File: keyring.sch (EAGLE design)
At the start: 7 parts, among them IC1 ATMEGA8-PU, T1 2N2222, X1 22-23-2031

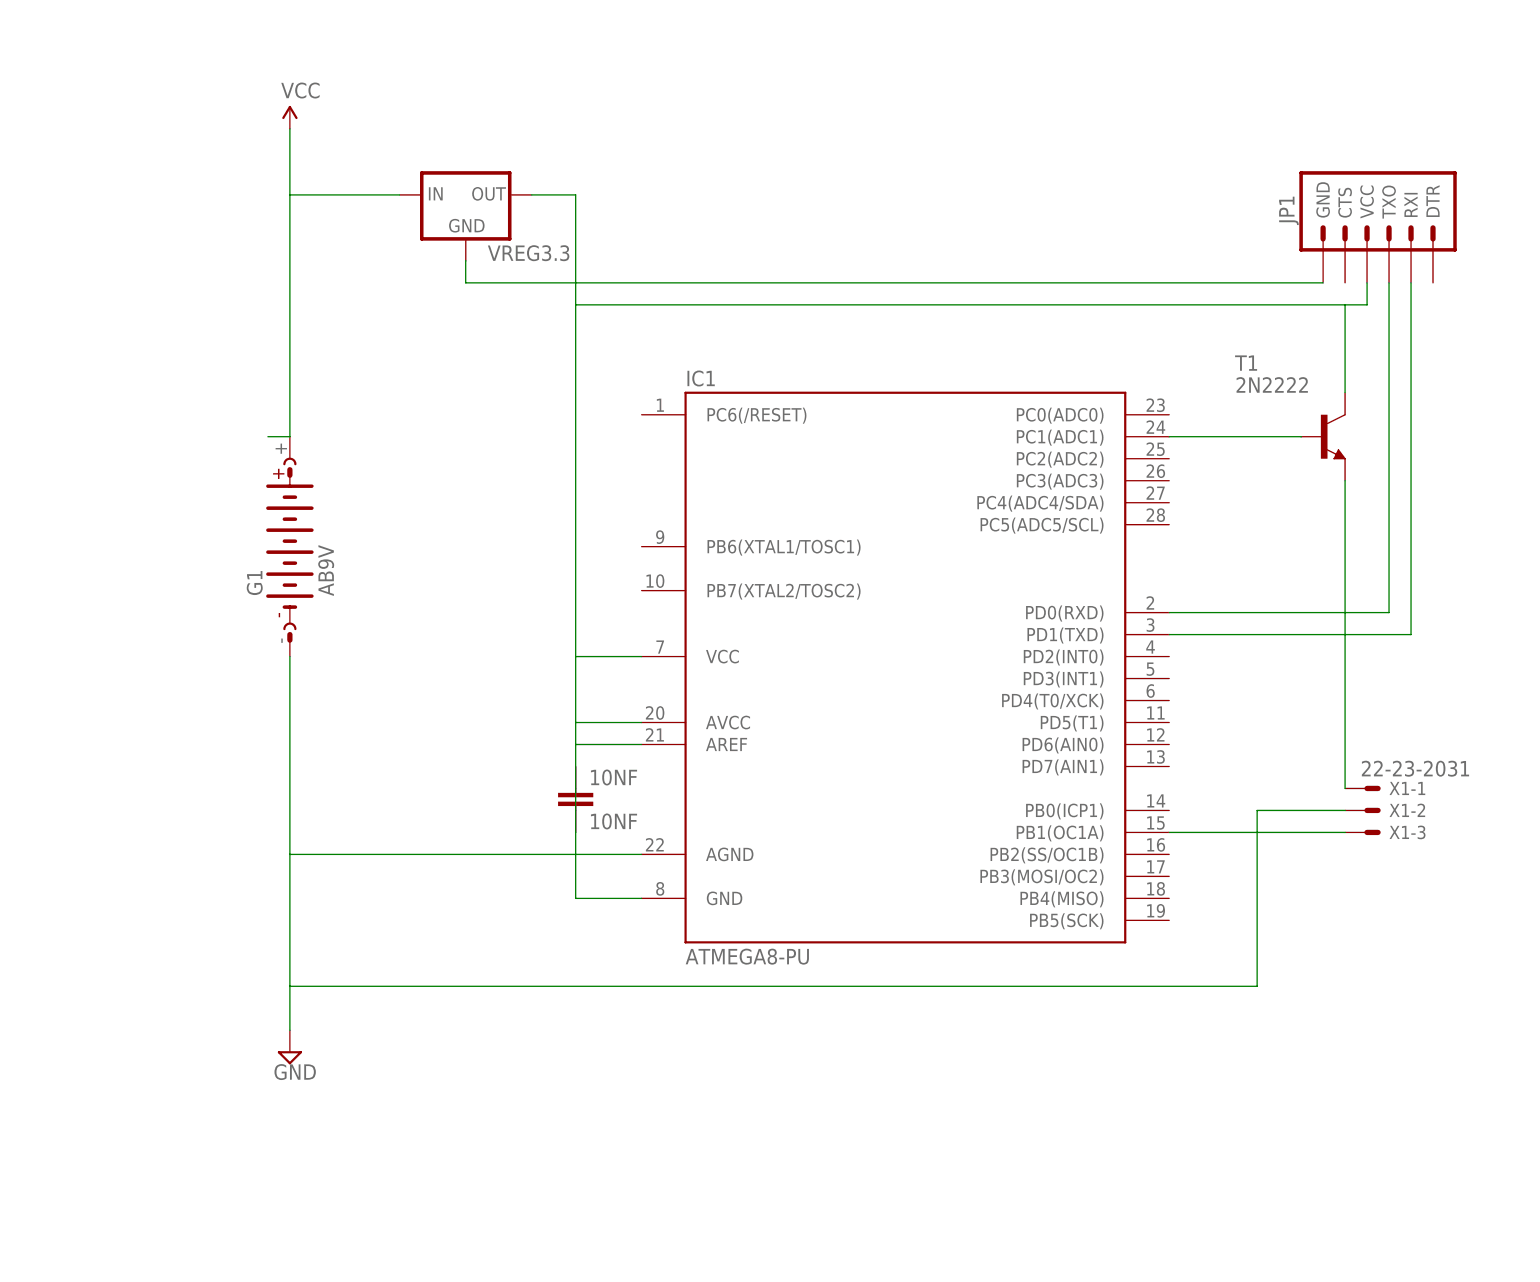
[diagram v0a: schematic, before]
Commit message: bigger pads
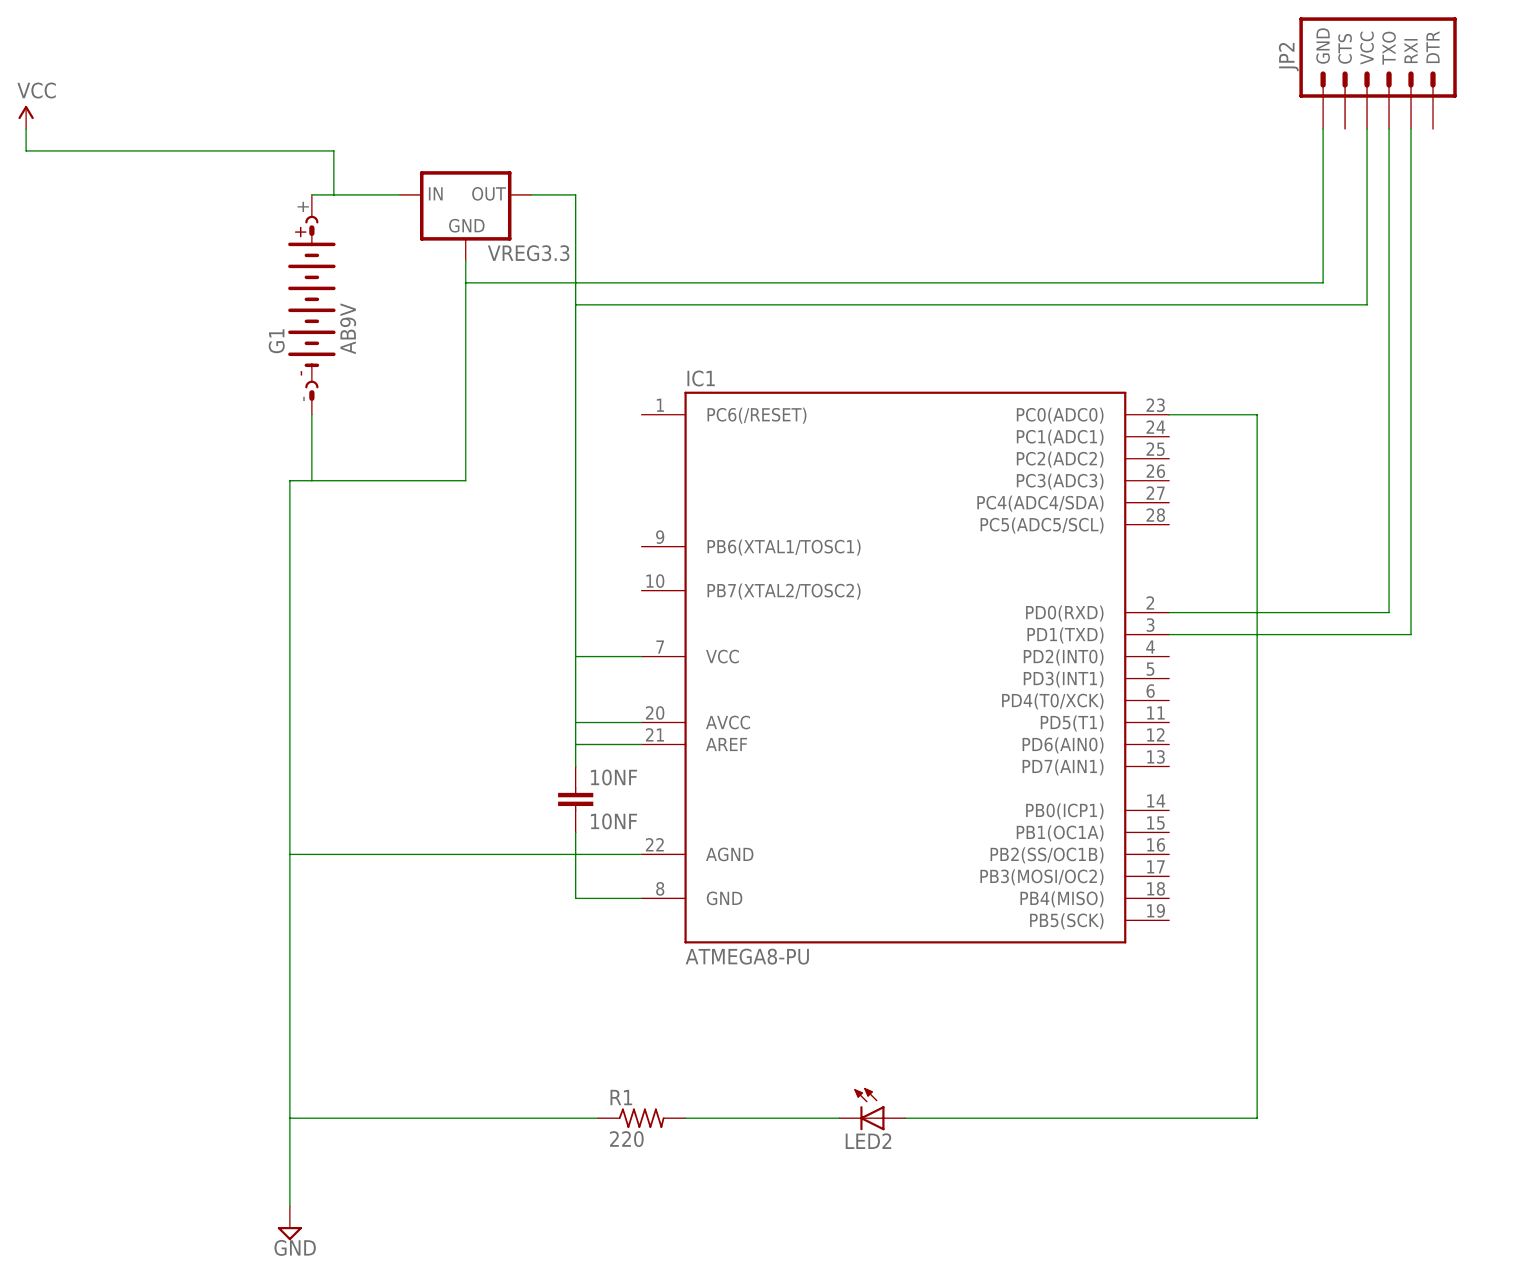
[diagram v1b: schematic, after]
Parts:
- removed JP1: (no value), SparkFun:ARDUINO_SERIAL_PROGRAMPTH
- removed T1: 2N2222, adafruit:2N2222
- removed X1: 22-23-2031, con-molex:22-23-2031
- added JP2: (no value), SparkFun:ARDUINO_SERIAL_PROGRAMLONGPADS
- added LED2: (no value), led:LED3MM
- added R1: 220, resistor:R-US_0207/12
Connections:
- removed net N$1: VREG3.3.GND
- removed net N$4: IC1.PC1(ADC1), T1.B
- removed net N$6: IC1.PB1(OC1A), X1-3.S
- new net N$7: LED2.C, R1.2
- new net N$8: 10NF.1, IC1.AREF, IC1.AVCC, IC1.VCC@1, JP2.VCC, VREG3.3.OUT
- net GND: now also JP2.GND, R1.1, VREG3.3.GND; no longer IC1.AREF, IC1.AVCC, IC1.VCC@1, JP1.VCC, T1.C, VREG3.3.OUT, X1-2.S
- net N$2: now also JP2.RXI; no longer JP1.RXI
- net N$3: now also JP2.TXO; no longer JP1.TXO
- net N$5: now also IC1.PC0(ADC0), LED2.A; no longer T1.E, X1-1.S
- net VCC: now also G1.+
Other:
- moved on the sheet: G1

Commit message: added keyboard
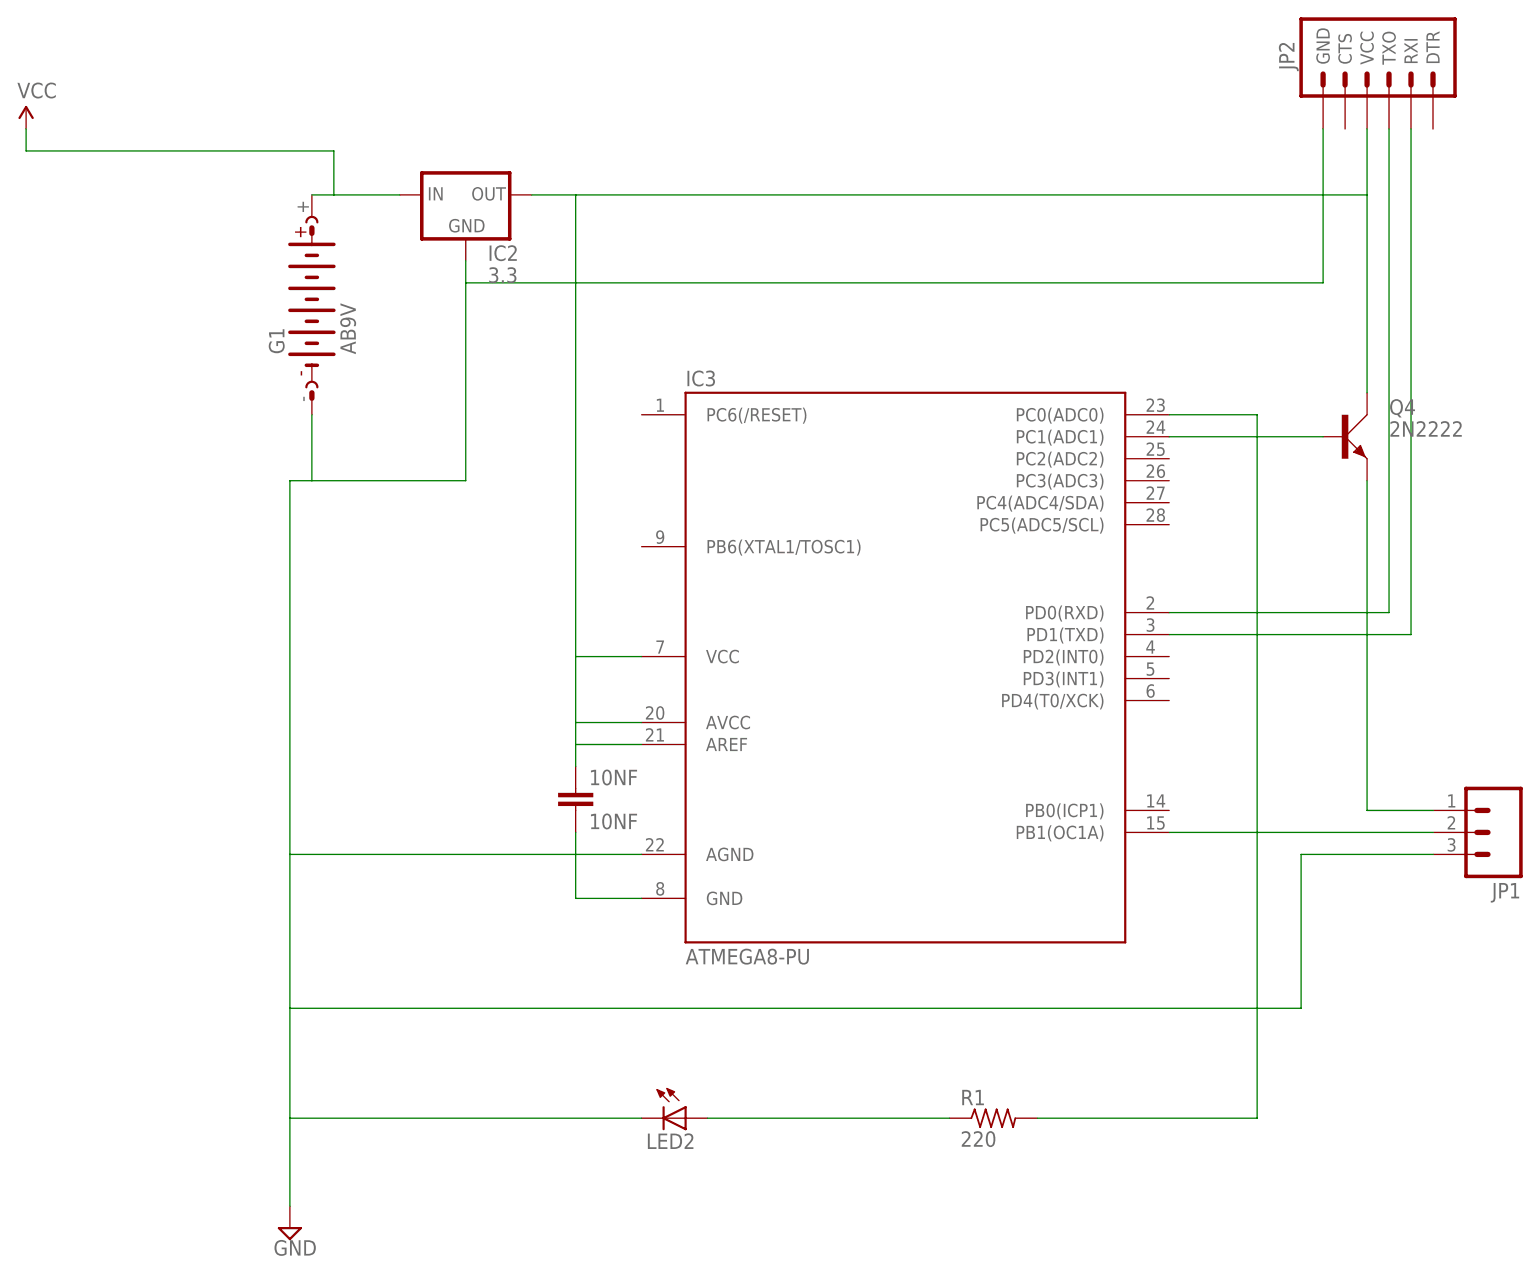
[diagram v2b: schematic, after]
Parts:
- removed IC1: ATMEGA8-PU, atmega8:ATMEGA8-PU
- added IC3: ATMEGA8-PU, atmega8 uden ben:ATMEGA8-PU
- added JP1: (no value), SparkFun:M03LONGPADS
- added Q4: 2N2222, transistor-small-signal:2N2222
- IC2: value (none) -> 3.3
- renumbered VREG3.3 to IC2
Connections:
- removed net GND: 10NF.2, G1.-, IC1.AGND, IC1.GND@1, IC2.GND, JP2.GND, R1.1
- new net N$1: IC3.PC1(ADC1), Q4.B
- new net N$10: 10NF.2, G1.-, IC2.GND, IC3.AGND, IC3.GND@1, JP1.VCC, JP2.GND, LED2.C
- new net N$4: JP1.OUT, Q4.E
- new net N$6: IC3.PB1(OC1A), JP1.GND
- net N$2: now also IC3.PD1(TXD); no longer IC1.PD1(TXD)
- net N$3: now also IC3.PD0(RXD); no longer IC1.PD0(RXD)
- net N$5: now also IC3.PC0(ADC0), R1.2; no longer IC1.PC0(ADC0), LED2.A
- net N$7: now also LED2.A, R1.1; no longer LED2.C, R1.2
- net N$8: now also IC3.AREF, IC3.AVCC, IC3.VCC@1, Q4.C; no longer IC1.AREF, IC1.AVCC, IC1.VCC@1
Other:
- moved on the sheet: LED2, R1
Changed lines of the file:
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@@
 </classes>
 <parts>
-<part name="IC1" library="atmega8" deviceset="ATMEGA8-PU" device=""/>
-<part name="VREG3.3" library="SparkFun" deviceset="V_REG_78XX" device="SINK"/>
 <part name="BATTERY" library="SparkFun" deviceset="VCC" device=""/>
 <part name="SUPPLY1" library="supply2" deviceset="GND" device=""/>
@@
 <part name="LED2" library="led" deviceset="LED" device="3MM"/>
 <part name="JP2" library="SparkFun" deviceset="ARDUINO_SERIAL_PROGRAM" device="LONGPADS"/>
+<part name="IC2" library="SparkFun" deviceset="V_REG_78XX" device="SINK" value="3.3"/>
+<part name="JP1" library="SparkFun" deviceset="M03" device="LONGPADS"/>
+<part name="IC3" library="atmega8 uden ben" deviceset="ATMEGA8-PU" device=""/>
+<part name="Q4" library="transistor-small-signal" deviceset="2N2222" device=""/>
 </parts>
 <sheets>
@@
 </plain>
 <instances>
-<instance part="IC1" gate="1" x="71.12" y="15.24"/>
-<instance part="VREG3.3" gate="G$1" x="20.32" y="68.58"/>
 <instance part="BATTERY" gate="1" x="-30.48" y="76.2"/>
 <instance part="SUPPLY1" gate="GND" x="0" y="-50.8"/>
 <instance part="10NF" gate="G$1" x="33.02" y="0"/>
 <instance part="G1" gate="G$1" x="2.54" y="55.88" rot="R90"/>
-<instance part="R1" gate="G$1" x="40.64" y="-38.1"/>
-<instance part="LED2" gate="G$1" x="68.58" y="-38.1" rot="R270"/>
+<instance part="R1" gate="G$1" x="81.28" y="-38.1"/>
+<instance part="LED2" gate="G$1" x="45.72" y="-38.1" rot="R270"/>
 <instance part="JP2" gate="G$1" x="127" y="81.28" rot="MR270"/>
+<instance part="IC2" gate="G$1" x="20.32" y="68.58"/>
+<instance part="JP1" gate="G$1" x="139.7" y="-5.08" rot="R180"/>
+<instance part="IC3" gate="1" x="71.12" y="15.24"/>
+<instance part="Q4" gate="1" x="121.92" y="40.64"/>
 </instances>
 <busses>
@@
 <wire x1="-30.48" y1="73.66" x2="5.08" y2="73.66" width="0.1524" layer="91"/>
 <wire x1="5.08" y1="73.66" x2="5.08" y2="68.58" width="0.1524" layer="91"/>
-<pinref part="VREG3.3" gate="G$1" pin="IN"/>
 <wire x1="5.08" y1="68.58" x2="12.7" y2="68.58" width="0.1524" layer="91"/>
 <pinref part="G1" gate="G$1" pin="+"/>
 <wire x1="2.54" y1="68.58" x2="5.08" y2="68.58" width="0.1524" layer="91"/>
+<pinref part="IC2" gate="G$1" pin="IN"/>
 </segment>
 </net>
-<net name="GND" class="0">
+<net name="N$10" class="0">
 <segment>
 <pinref part="SUPPLY1" gate="GND" pin="GND"/>
 <wire x1="0" y1="35.56" x2="0" y2="-7.62" width="0.1524" layer="91"/>
-<wire x1="0" y1="-7.62" x2="0" y2="-38.1" width="0.1524" layer="91"/>
-<pinref part="IC1" gate="1" pin="AGND"/>
+<wire x1="0" y1="-7.62" x2="0" y2="-25.4" width="0.1524" layer="91"/>
+<wire x1="0" y1="-25.4" x2="0" y2="-38.1" width="0.1524" layer="91"/>
 <wire x1="0" y1="-38.1" x2="0" y2="-48.26" width="0.1524" layer="91"/>
 <wire x1="40.64" y1="-7.62" x2="33.02" y2="-7.62" width="0.1524" layer="91"/>
 <wire x1="33.02" y1="-7.62" x2="0" y2="-7.62" width="0.1524" layer="91"/>
-<pinref part="IC1" gate="1" pin="GND@1"/>
 <wire x1="40.64" y1="-12.7" x2="33.02" y2="-12.7" width="0.1524" layer="91"/>
 <wire x1="33.02" y1="-12.7" x2="33.02" y2="-7.62" width="0.1524" layer="91"/>
@@
 <wire x1="33.02" y1="-5.08" x2="33.02" y2="-7.62" width="0.1524" layer="91"/>
 <wire x1="0" y1="35.56" x2="2.54" y2="35.56" width="0.1524" layer="91"/>
-<pinref part="VREG3.3" gate="G$1" pin="GND"/>
 <wire x1="2.54" y1="35.56" x2="20.32" y2="35.56" width="0.1524" layer="91"/>
 <wire x1="20.32" y1="58.42" x2="20.32" y2="60.96" width="0.1524" layer="91"/>
@@
 <pinref part="G1" gate="G$1" pin="-"/>
 <wire x1="2.54" y1="43.18" x2="2.54" y2="35.56" width="0.1524" layer="91"/>
-<pinref part="R1" gate="G$1" pin="1"/>
-<wire x1="35.56" y1="-38.1" x2="0" y2="-38.1" width="0.1524" layer="91"/>
 <pinref part="JP2" gate="G$1" pin="GND"/>
 <wire x1="119.38" y1="58.42" x2="119.38" y2="76.2" width="0.1524" layer="91"/>
+<pinref part="IC2" gate="G$1" pin="GND"/>
+<wire x1="0" y1="-25.4" x2="116.84" y2="-25.4" width="0.1524" layer="91"/>
+<wire x1="116.84" y1="-25.4" x2="116.84" y2="-7.62" width="0.1524" layer="91"/>
+<pinref part="IC3" gate="1" pin="GND@1"/>
+<pinref part="IC3" gate="1" pin="AGND"/>
+<pinref part="LED2" gate="G$1" pin="C"/>
+<wire x1="40.64" y1="-38.1" x2="0" y2="-38.1" width="0.1524" layer="91"/>
+<pinref part="JP1" gate="G$1" pin="VCC"/>
+<wire x1="132.08" y1="-7.62" x2="116.84" y2="-7.62" width="0.1524" layer="91"/>
 </segment>
 </net>
 <net name="N$2" class="0">
 <segment>
-<pinref part="IC1" gate="1" pin="PD1(TXD)"/>
 <wire x1="129.54" y1="17.78" x2="101.6" y2="17.78" width="0.1524" layer="91"/>
 <wire x1="129.54" y1="76.2" x2="129.54" y2="17.78" width="0.1524" layer="91"/>
 <pinref part="JP2" gate="G$1" pin="RXI"/>
+<pinref part="IC3" gate="1" pin="PD1(TXD)"/>
 </segment>
 </net>
 <net name="N$3" class="0">
 <segment>
-<pinref part="IC1" gate="1" pin="PD0(RXD)"/>
 <wire x1="127" y1="20.32" x2="101.6" y2="20.32" width="0.1524" layer="91"/>
 <wire x1="127" y1="76.2" x2="127" y2="20.32" width="0.1524" layer="91"/>
 <pinref part="JP2" gate="G$1" pin="TXO"/>
+<pinref part="IC3" gate="1" pin="PD0(RXD)"/>
 </segment>
 </net>
 <net name="N$5" class="0">
 <segment>
-<wire x1="71.12" y1="-38.1" x2="111.76" y2="-38.1" width="0.1524" layer="91"/>
 <wire x1="111.76" y1="-38.1" x2="111.76" y2="43.18" width="0.1524" layer="91"/>
-<pinref part="IC1" gate="1" pin="PC0(ADC0)"/>
 <wire x1="111.76" y1="43.18" x2="101.6" y2="43.18" width="0.1524" layer="91"/>
-<pinref part="LED2" gate="G$1" pin="A"/>
-</segment>
-</net>
-<net name="N$7" class="0">
-<segment>
-<wire x1="45.72" y1="-38.1" x2="63.5" y2="-38.1" width="0.1524" layer="91"/>
+<pinref part="IC3" gate="1" pin="PC0(ADC0)"/>
 <pinref part="R1" gate="G$1" pin="2"/>
-<pinref part="LED2" gate="G$1" pin="C"/>
+<wire x1="111.76" y1="-38.1" x2="86.36" y2="-38.1" width="0.1524" layer="91"/>
 </segment>
 </net>
 <net name="N$8" class="0">
 <segment>
-<pinref part="IC1" gate="1" pin="AVCC"/>
-<pinref part="VREG3.3" gate="G$1" pin="OUT"/>
 <wire x1="27.94" y1="68.58" x2="33.02" y2="68.58" width="0.1524" layer="91"/>
-<wire x1="33.02" y1="68.58" x2="33.02" y2="55.88" width="0.1524" layer="91"/>
-<wire x1="124.46" y1="55.88" x2="33.02" y2="55.88" width="0.1524" layer="91"/>
-<wire x1="33.02" y1="55.88" x2="33.02" y2="15.24" width="0.1524" layer="91"/>
-<pinref part="IC1" gate="1" pin="VCC@1"/>
+<wire x1="33.02" y1="68.58" x2="33.02" y2="15.24" width="0.1524" layer="91"/>
 <wire x1="40.64" y1="15.24" x2="33.02" y2="15.24" width="0.1524" layer="91"/>
 <wire x1="33.02" y1="15.24" x2="33.02" y2="7.62" width="0.1524" layer="91"/>
 <wire x1="33.02" y1="7.62" x2="40.64" y2="7.62" width="0.1524" layer="91"/>
-<pinref part="IC1" gate="1" pin="AREF"/>
 <wire x1="40.64" y1="5.08" x2="33.02" y2="5.08" width="0.1524" layer="91"/>
 <wire x1="33.02" y1="5.08" x2="33.02" y2="7.62" width="0.1524" layer="91"/>
@@
 <wire x1="33.02" y1="2.54" x2="33.02" y2="5.08" width="0.1524" layer="91"/>
 <pinref part="JP2" gate="G$1" pin="VCC"/>
-<wire x1="124.46" y1="55.88" x2="124.46" y2="76.2" width="0.1524" layer="91"/>
+<pinref part="IC2" gate="G$1" pin="OUT"/>
+<wire x1="124.46" y1="68.58" x2="124.46" y2="76.2" width="0.1524" layer="91"/>
+<wire x1="33.02" y1="68.58" x2="124.46" y2="68.58" width="0.1524" layer="91"/>
+<wire x1="124.46" y1="45.72" x2="124.46" y2="68.58" width="0.1524" layer="91"/>
+<pinref part="IC3" gate="1" pin="VCC@1"/>
+<pinref part="IC3" gate="1" pin="AREF"/>
+<pinref part="IC3" gate="1" pin="AVCC"/>
+<pinref part="Q4" gate="1" pin="C"/>
 </segment>
 </net>
+<net name="N$1" class="0">
+<segment>
+<wire x1="101.6" y1="40.64" x2="119.38" y2="40.64" width="0.1524" layer="91"/>
+<pinref part="IC3" gate="1" pin="PC1(ADC1)"/>
+<pinref part="Q4" gate="1" pin="B"/>
+</segment>
+</net>
+<net name="N$4" class="0">
+<segment>
+<wire x1="124.46" y1="35.56" x2="124.46" y2="-2.54" width="0.1524" layer="91"/>
+<pinref part="JP1" gate="G$1" pin="OUT"/>
+<wire x1="132.08" y1="-2.54" x2="124.46" y2="-2.54" width="0.1524" layer="91"/>
+<pinref part="Q4" gate="1" pin="E"/>
+</segment>
+</net>
+<net name="N$7" class="0">
+<segment>
+<pinref part="R1" gate="G$1" pin="1"/>
+<pinref part="LED2" gate="G$1" pin="A"/>
+<wire x1="76.2" y1="-38.1" x2="48.26" y2="-38.1" width="0.1524" layer="91"/>
+</segment>
+</net>
+<net name="N$6" class="0">
+<segment>
+<wire x1="101.6" y1="-5.08" x2="132.08" y2="-5.08" width="0.1524" layer="91"/>
+<pinref part="JP1" gate="G$1" pin="GND"/>
+<pinref part="IC3" gate="1" pin="PB1(OC1A)"/>
+</segment>
+</net>
